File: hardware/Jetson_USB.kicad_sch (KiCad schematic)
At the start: 17 parts, among them J2 USB_C_Receptacle_USB2.0_16P, U3 FT230XS, U6 USBLC6-2SC6

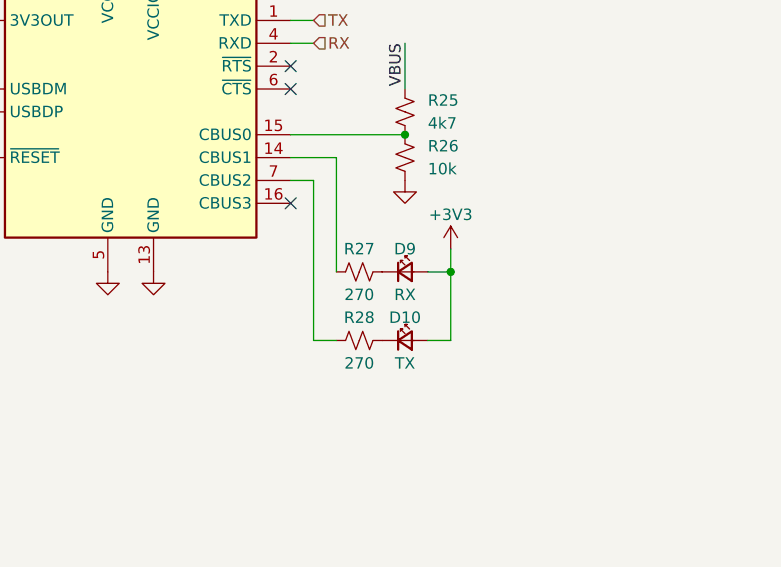
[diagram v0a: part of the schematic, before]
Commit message: Add fan headers and place components
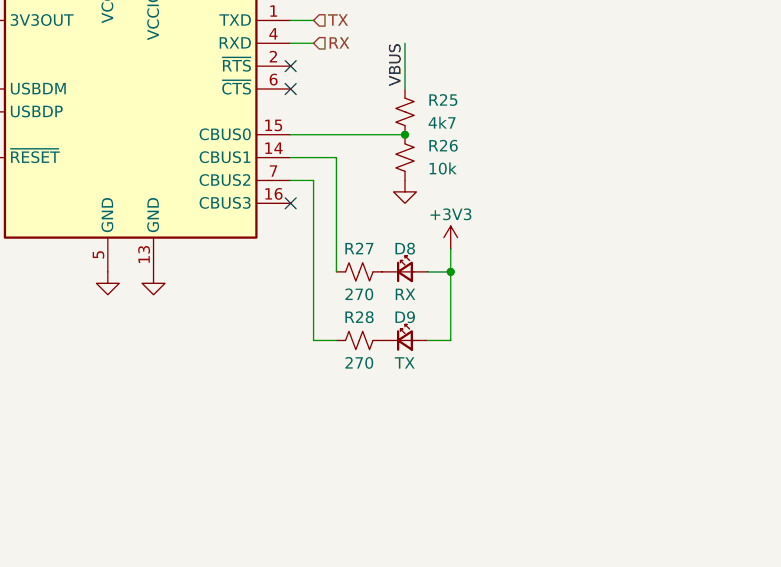
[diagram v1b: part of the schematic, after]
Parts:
- renumbered D9 to D8, D10 to D9
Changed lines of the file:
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@@
   (symbol (lib_id "Device:LED_Small") (at 184.15 106.68 0) (unit 1)
     (in_bom yes) (on_board yes) (dnp no)
-    (property "Reference" "D9" (at 184.15 104.14 0)
+    (property "Reference" "D8" (at 184.15 104.14 0)
       (effects (font (size 1.27 1.27)))
     )
@@
       (project "AMP_PCBv3"
         (path "/b0eed686-2b97-4c99-952c-ca5393e47dfe/6380782e-102d-41fe-b761-8a0fbdc976b4"
-          (reference "D9") (unit 1)
+          (reference "D8") (unit 1)
         )
       )
@@
   (symbol (lib_id "Device:LED_Small") (at 184.15 114.3 0) (unit 1)
     (in_bom yes) (on_board yes) (dnp no)
-    (property "Reference" "D10" (at 184.15 111.76 0)
+    (property "Reference" "D9" (at 184.15 111.76 0)
       (effects (font (size 1.27 1.27)))
     )
@@
       (project "AMP_PCBv3"
         (path "/b0eed686-2b97-4c99-952c-ca5393e47dfe/6380782e-102d-41fe-b761-8a0fbdc976b4"
-          (reference "D10") (unit 1)
+          (reference "D9") (unit 1)
         )
       )

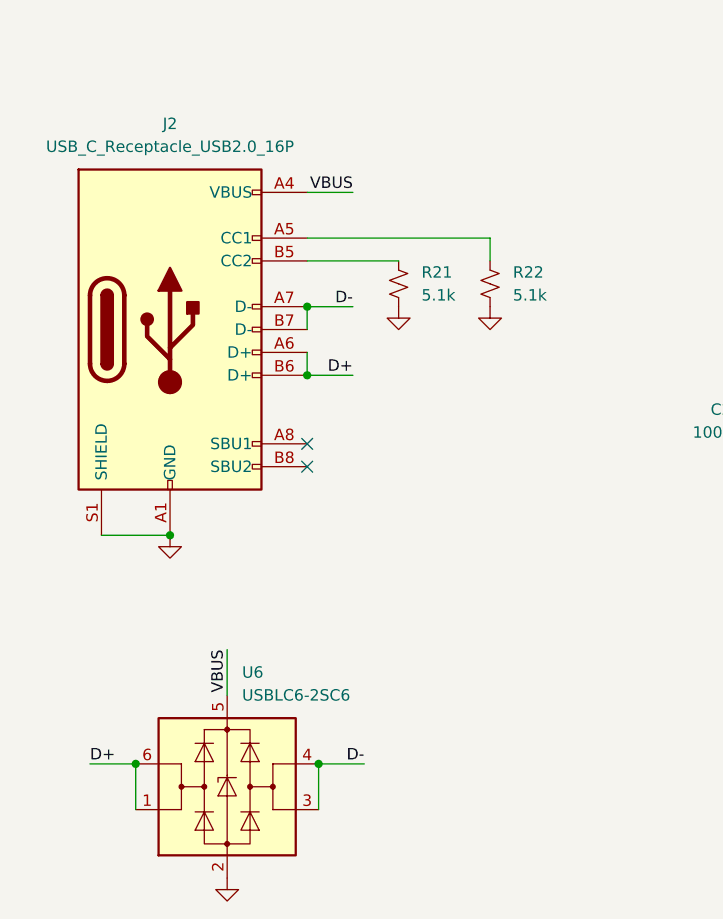
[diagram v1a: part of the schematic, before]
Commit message: Add steering connector and route board (4 layers)
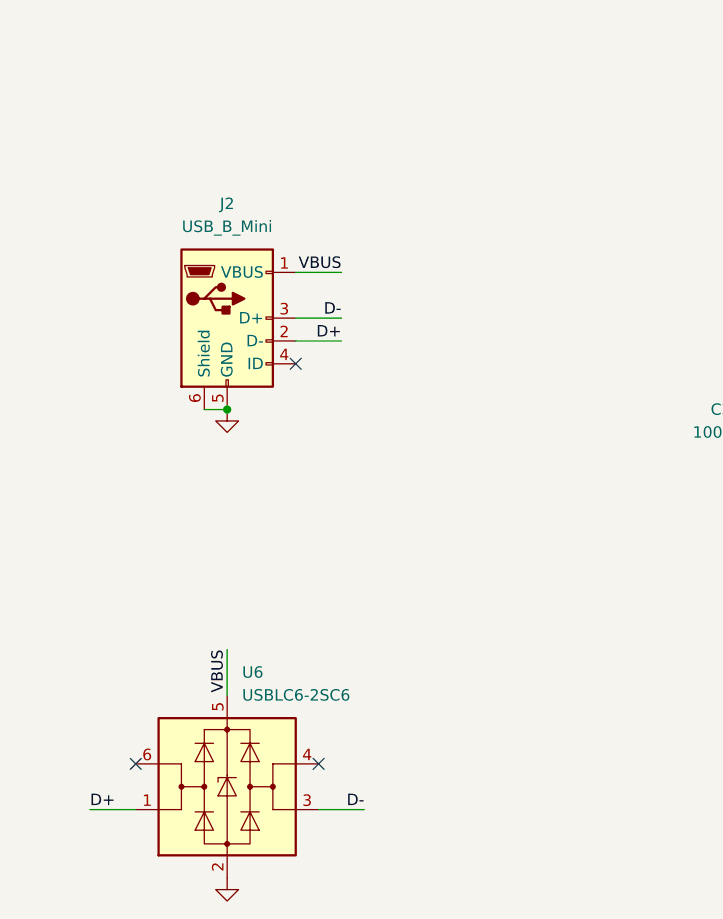
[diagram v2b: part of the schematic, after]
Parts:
- removed J2: USB_C_Receptacle_USB2.0_16P, AMP_Custom:USB_C_Receptacle_GCT_USB4145, symbol Connector:USB_C_Receptacle_USB2.0_16P
- removed R21, R22: 5.1k, Resistor_SMD:R_0805_2012Metric_Pad1.20x1.40mm_HandSolder, symbol Device:R_Small_US
- added J2: USB_B_Mini, AMP_Custom:USB_Mini-B_Adam_Tech_MUSB-B5-S-VT-02_Vertical_CircularHoles, symbol Connector:USB_B_Mini
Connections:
- net D+: now also J2.2 (D-); no longer U6.6 (I/O1)
- net D-: now also J2.3 (D+); no longer U6.4 (I/O2)
- net GND: now also J2.5 (GND), J2.6 (Shield)
- net VBUS: now also J2.1 (VBUS)
- no-connect marks 5 -> 6

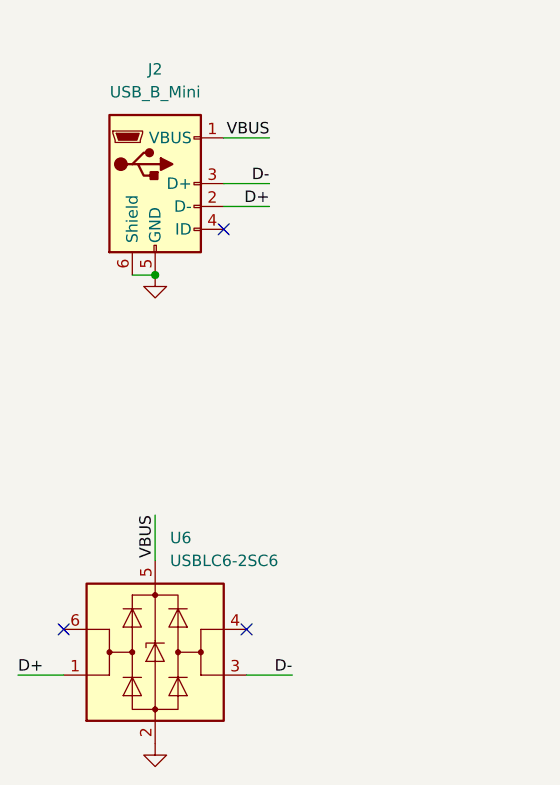
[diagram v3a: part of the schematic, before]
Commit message: Resize board and begin new layout
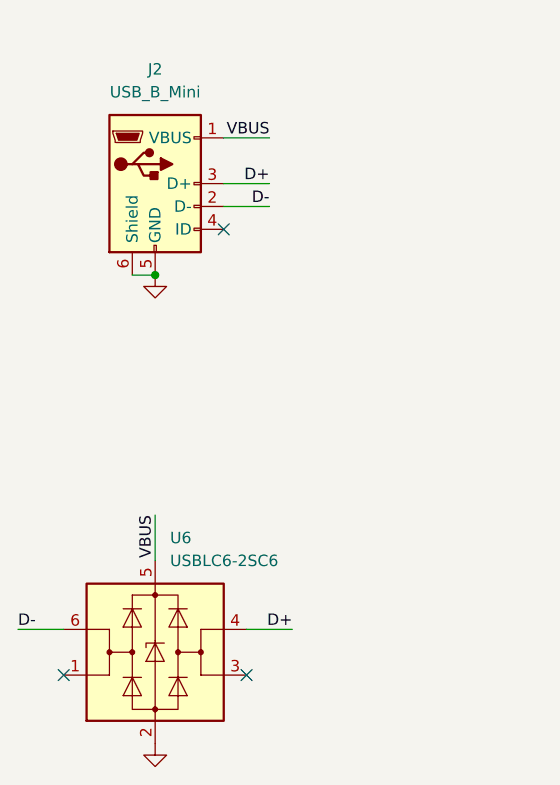
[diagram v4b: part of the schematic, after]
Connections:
- net D+: now also J2.3 (D+), U6.4 (I/O2); no longer J2.2 (D-), U6.1 (I/O1)
- net D-: now also J2.2 (D-), U6.6 (I/O1); no longer J2.3 (D+), U6.3 (I/O2)
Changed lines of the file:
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@@
-	)
-	(no_connect
-		(at 68.58 138.43)
 	)
 	(no_connect
@@
 	)
 	(no_connect
-		(at 48.26 138.43)
+		(at 68.58 143.51)
 	)
 	(no_connect
@@
 		(at 171.45 99.06)
 	)
+	(no_connect
+		(at 48.26 143.51)
+	)
 	(wire
 		(pts
@@
 	(wire
 		(pts
-			(xy 68.58 143.51) (xy 73.66 143.51)
+			(xy 68.58 138.43) (xy 73.66 138.43)
 		)
 		(stroke
@@
 	(wire
 		(pts
-			(xy 48.26 143.51) (xy 43.18 143.51)
+			(xy 48.26 138.43) (xy 43.18 138.43)
 		)
 		(stroke
@@
 	)
 	(label "D+"
-		(at 43.18 143.51 0)
-		(fields_autoplaced yes)
-		(effects
-			(font
-				(size 1.27 1.27)
-			)
-			(justify left bottom)
+		(at 73.66 138.43 180)
+		(fields_autoplaced yes)
+		(effects
+			(font
+				(size 1.27 1.27)
+			)
+			(justify right bottom)
 		)
 	)
@@
 		)
 	)
+	(label "D+"
+		(at 71.12 88.9 180)
+		(fields_autoplaced yes)
+		(effects
+			(font
+				(size 1.27 1.27)
+			)
+			(justify right bottom)
+		)
+	)
 	(label "D-"
-		(at 71.12 88.9 180)
-		(fields_autoplaced yes)
-		(effects
-			(font
-				(size 1.27 1.27)
-			)
-			(justify right bottom)
-		)
-	)
-	(label "D+"
 		(at 71.12 91.44 180)
 		(fields_autoplaced yes)
@@
 	)
 	(label "D-"
-		(at 73.66 143.51 180)
-		(fields_autoplaced yes)
-		(effects
-			(font
-				(size 1.27 1.27)
-			)
-			(justify right bottom)
-		)
-	)
+		(at 43.18 138.43 0)
+		(fields_autoplaced yes)
+		(effects
+			(font
+				(size 1.27 1.27)
+			)
+			(justify left bottom)
+		)
+	)

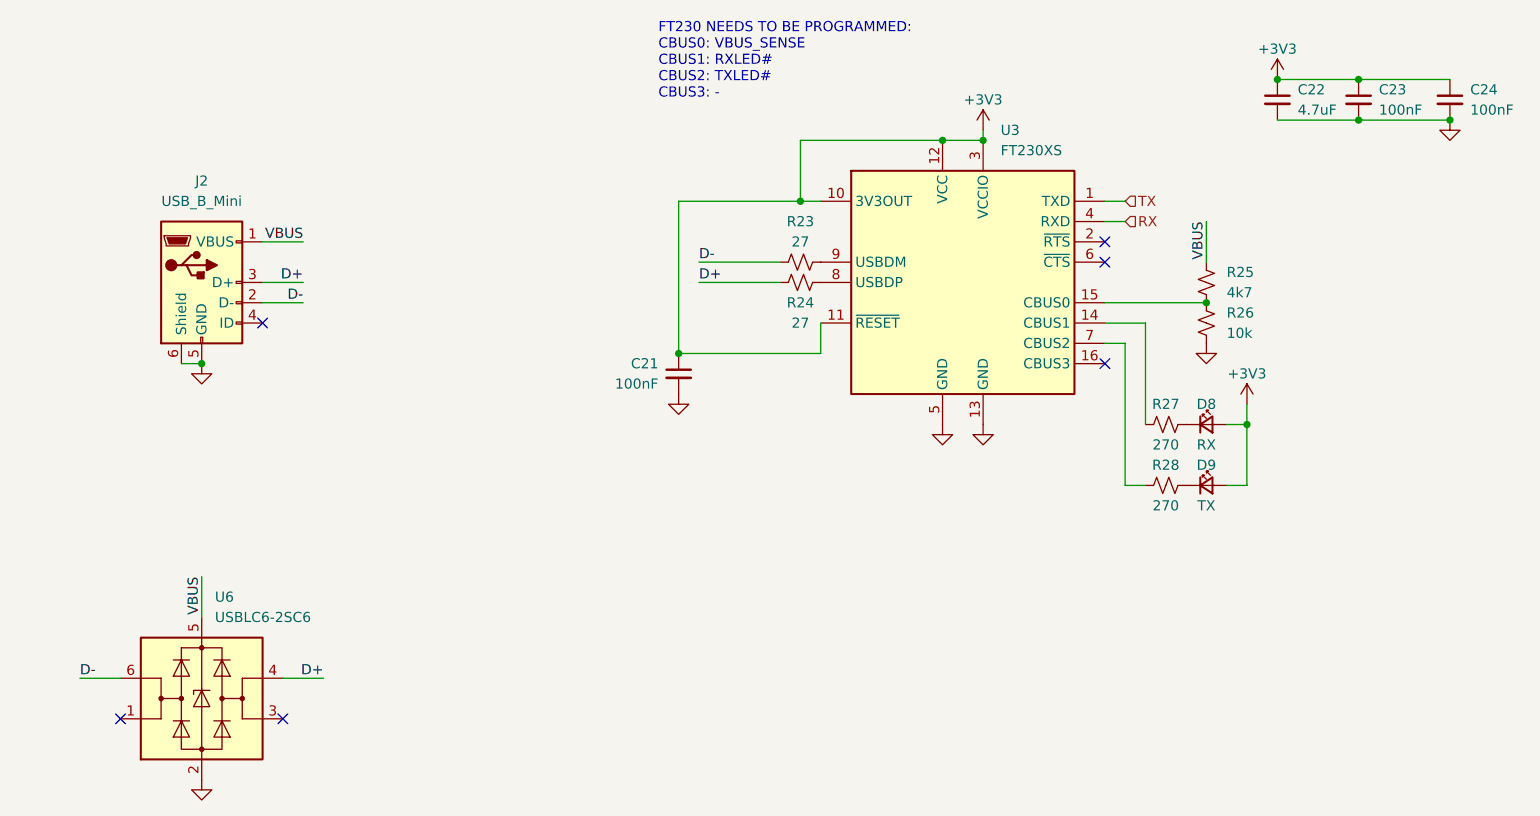
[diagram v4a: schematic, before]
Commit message: Add level shifter for LEDs
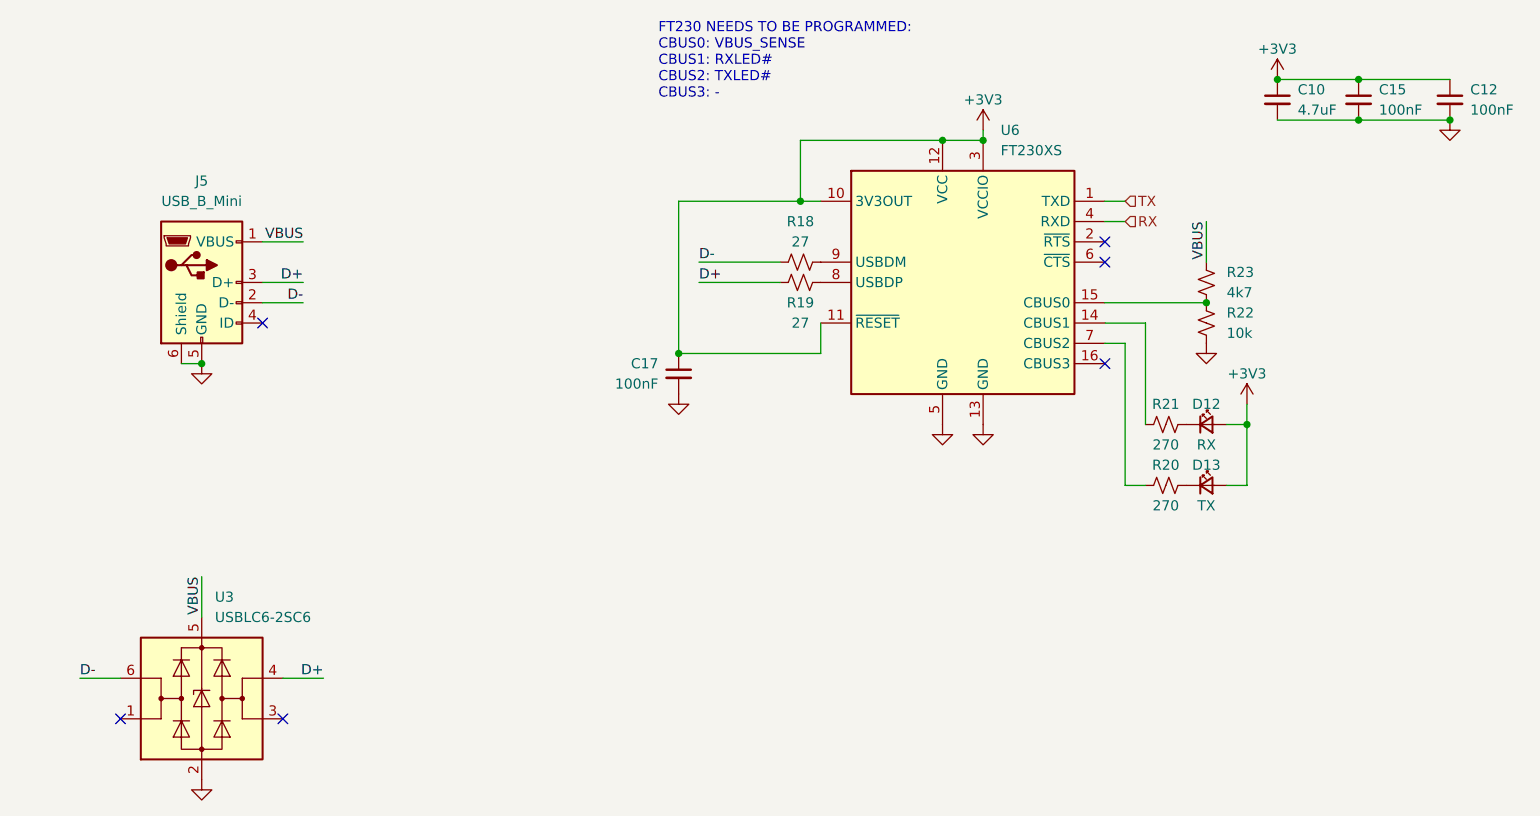
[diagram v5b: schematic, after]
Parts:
- renumbered C22 to C10, C24 to C12, C23 to C15, C21 to C17, D8 to D12, D9 to D13, J2 to J5, R23 to R18, R24 to R19, R28 to R20, R27 to R21, R26 to R22, R25 to R23, U6 to U3, U3 to U6
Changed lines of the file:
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@@
 		(dnp no)
 		(fields_autoplaced yes)
-		(property "Reference" "J2"
+		(property "Reference" "J5"
 			(at 58.42 76.2 0)
 			(effects
@@
 			(project "AMP_PCBv3"
 				(path "/b0eed686-2b97-4c99-952c-ca5393e47dfe/6380782e-102d-41fe-b761-8a0fbdc976b4"
-					(reference "J2")
+					(reference "J5")
 					(unit 1)
 				)
@@
 		(on_board yes)
 		(dnp no)
-		(property "Reference" "C22"
+		(property "Reference" "C10"
 			(at 195.58 64.7763 0)
 			(effects
@@
 			(project "AMP_PCBv3"
 				(path "/b0eed686-2b97-4c99-952c-ca5393e47dfe/6380782e-102d-41fe-b761-8a0fbdc976b4"
-					(reference "C22")
+					(reference "C10")
 					(unit 1)
 				)
@@
 		(on_board yes)
 		(dnp no)
-		(property "Reference" "C21"
+		(property "Reference" "C17"
 			(at 115.57 99.06 0)
 			(effects
@@
 			(project "AMP_PCBv3"
 				(path "/b0eed686-2b97-4c99-952c-ca5393e47dfe/6380782e-102d-41fe-b761-8a0fbdc976b4"
-					(reference "C21")
+					(reference "C17")
 					(unit 1)
 				)
@@
 		(on_board yes)
 		(dnp no)
-		(property "Reference" "C23"
+		(property "Reference" "C15"
 			(at 205.74 64.7763 0)
 			(effects
@@
 			(project "AMP_PCBv3"
 				(path "/b0eed686-2b97-4c99-952c-ca5393e47dfe/6380782e-102d-41fe-b761-8a0fbdc976b4"
-					(reference "C23")
+					(reference "C15")
 					(unit 1)
 				)
@@
 		(on_board yes)
 		(dnp no)
-		(property "Reference" "R23"
+		(property "Reference" "R18"
 			(at 133.35 81.28 90)
 			(effects
@@
 			(project "AMP_PCBv3"
 				(path "/b0eed686-2b97-4c99-952c-ca5393e47dfe/6380782e-102d-41fe-b761-8a0fbdc976b4"
-					(reference "R23")
+					(reference "R18")
 					(unit 1)
 				)
@@
 		(on_board yes)
 		(dnp no)
-		(property "Reference" "R24"
+		(property "Reference" "R19"
 			(at 133.35 91.44 90)
 			(effects
@@
 			(project "AMP_PCBv3"
 				(path "/b0eed686-2b97-4c99-952c-ca5393e47dfe/6380782e-102d-41fe-b761-8a0fbdc976b4"
-					(reference "R24")
+					(reference "R19")
 					(unit 1)
 				)
@@
 		(on_board yes)
 		(dnp no)
-		(property "Reference" "D8"
+		(property "Reference" "D12"
 			(at 184.15 104.14 0)
 			(effects
@@
 			(project "AMP_PCBv3"
 				(path "/b0eed686-2b97-4c99-952c-ca5393e47dfe/6380782e-102d-41fe-b761-8a0fbdc976b4"
-					(reference "D8")
+					(reference "D12")
 					(unit 1)
 				)
@@
 		(on_board yes)
 		(dnp no)
-		(property "Reference" "R28"
+		(property "Reference" "R20"
 			(at 179.07 111.76 90)
 			(effects
@@
 			(project "AMP_PCBv3"
 				(path "/b0eed686-2b97-4c99-952c-ca5393e47dfe/6380782e-102d-41fe-b761-8a0fbdc976b4"
-					(reference "R28")
+					(reference "R20")
 					(unit 1)
 				)
@@
 		(on_board yes)
 		(dnp no)
-		(property "Reference" "D9"
+		(property "Reference" "D13"
 			(at 184.15 111.76 0)
 			(effects
@@
 			(project "AMP_PCBv3"
 				(path "/b0eed686-2b97-4c99-952c-ca5393e47dfe/6380782e-102d-41fe-b761-8a0fbdc976b4"
-					(reference "D9")
+					(reference "D13")
 					(unit 1)
 				)
@@
 		(on_board yes)
 		(dnp no)
-		(property "Reference" "C24"
+		(property "Reference" "C12"
 			(at 217.17 64.7763 0)
 			(effects
@@
 			(project "AMP_PCBv3"
 				(path "/b0eed686-2b97-4c99-952c-ca5393e47dfe/6380782e-102d-41fe-b761-8a0fbdc976b4"
-					(reference "C24")
+					(reference "C12")
 					(unit 1)
 				)
@@
 		(dnp no)
 		(fields_autoplaced yes)
-		(property "Reference" "U6"
+		(property "Reference" "U3"
 			(at 60.0711 128.27 0)
 			(effects
@@
 			(project "AMP_PCBv3"
 				(path "/b0eed686-2b97-4c99-952c-ca5393e47dfe/6380782e-102d-41fe-b761-8a0fbdc976b4"
-					(reference "U6")
+					(reference "U3")
 					(unit 1)
 				)
@@
 		(dnp no)
 		(fields_autoplaced yes)
-		(property "Reference" "U3"
+		(property "Reference" "U6"
 			(at 158.4041 69.85 0)
 			(effects
@@
 			(project "AMP_PCBv3"
 				(path "/b0eed686-2b97-4c99-952c-ca5393e47dfe/6380782e-102d-41fe-b761-8a0fbdc976b4"
-					(reference "U3")
+					(reference "U6")
 					(unit 1)
 				)
@@
 		(dnp no)
 		(fields_autoplaced yes)
-		(property "Reference" "R26"
+		(property "Reference" "R22"
 			(at 186.69 92.71 0)
 			(effects
@@
 			(project "AMP_PCBv3"
 				(path "/b0eed686-2b97-4c99-952c-ca5393e47dfe/6380782e-102d-41fe-b761-8a0fbdc976b4"
-					(reference "R26")
+					(reference "R22")
 					(unit 1)
 				)
@@
 		(dnp no)
 		(fields_autoplaced yes)
-		(property "Reference" "R25"
+		(property "Reference" "R23"
 			(at 186.69 87.63 0)
 			(effects
@@
 			(project "AMP_PCBv3"
 				(path "/b0eed686-2b97-4c99-952c-ca5393e47dfe/6380782e-102d-41fe-b761-8a0fbdc976b4"
-					(reference "R25")
+					(reference "R23")
 					(unit 1)
 				)
@@
 		(on_board yes)
 		(dnp no)
-		(property "Reference" "R27"
+		(property "Reference" "R21"
 			(at 179.07 104.14 90)
 			(effects
@@
 			(project "AMP_PCBv3"
 				(path "/b0eed686-2b97-4c99-952c-ca5393e47dfe/6380782e-102d-41fe-b761-8a0fbdc976b4"
-					(reference "R27")
-					(unit 1)
-				)
+					(reference "R21")
+					(unit 1)
+				)
